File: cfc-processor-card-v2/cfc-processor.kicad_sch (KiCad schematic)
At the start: 11 parts, among them J1 TFM-120-01-L-D-RA, J2 2-1734592-0, J3 J-SAMTEC-TFM-110-X1-XXX-D-RA, J4 Conn_01x04

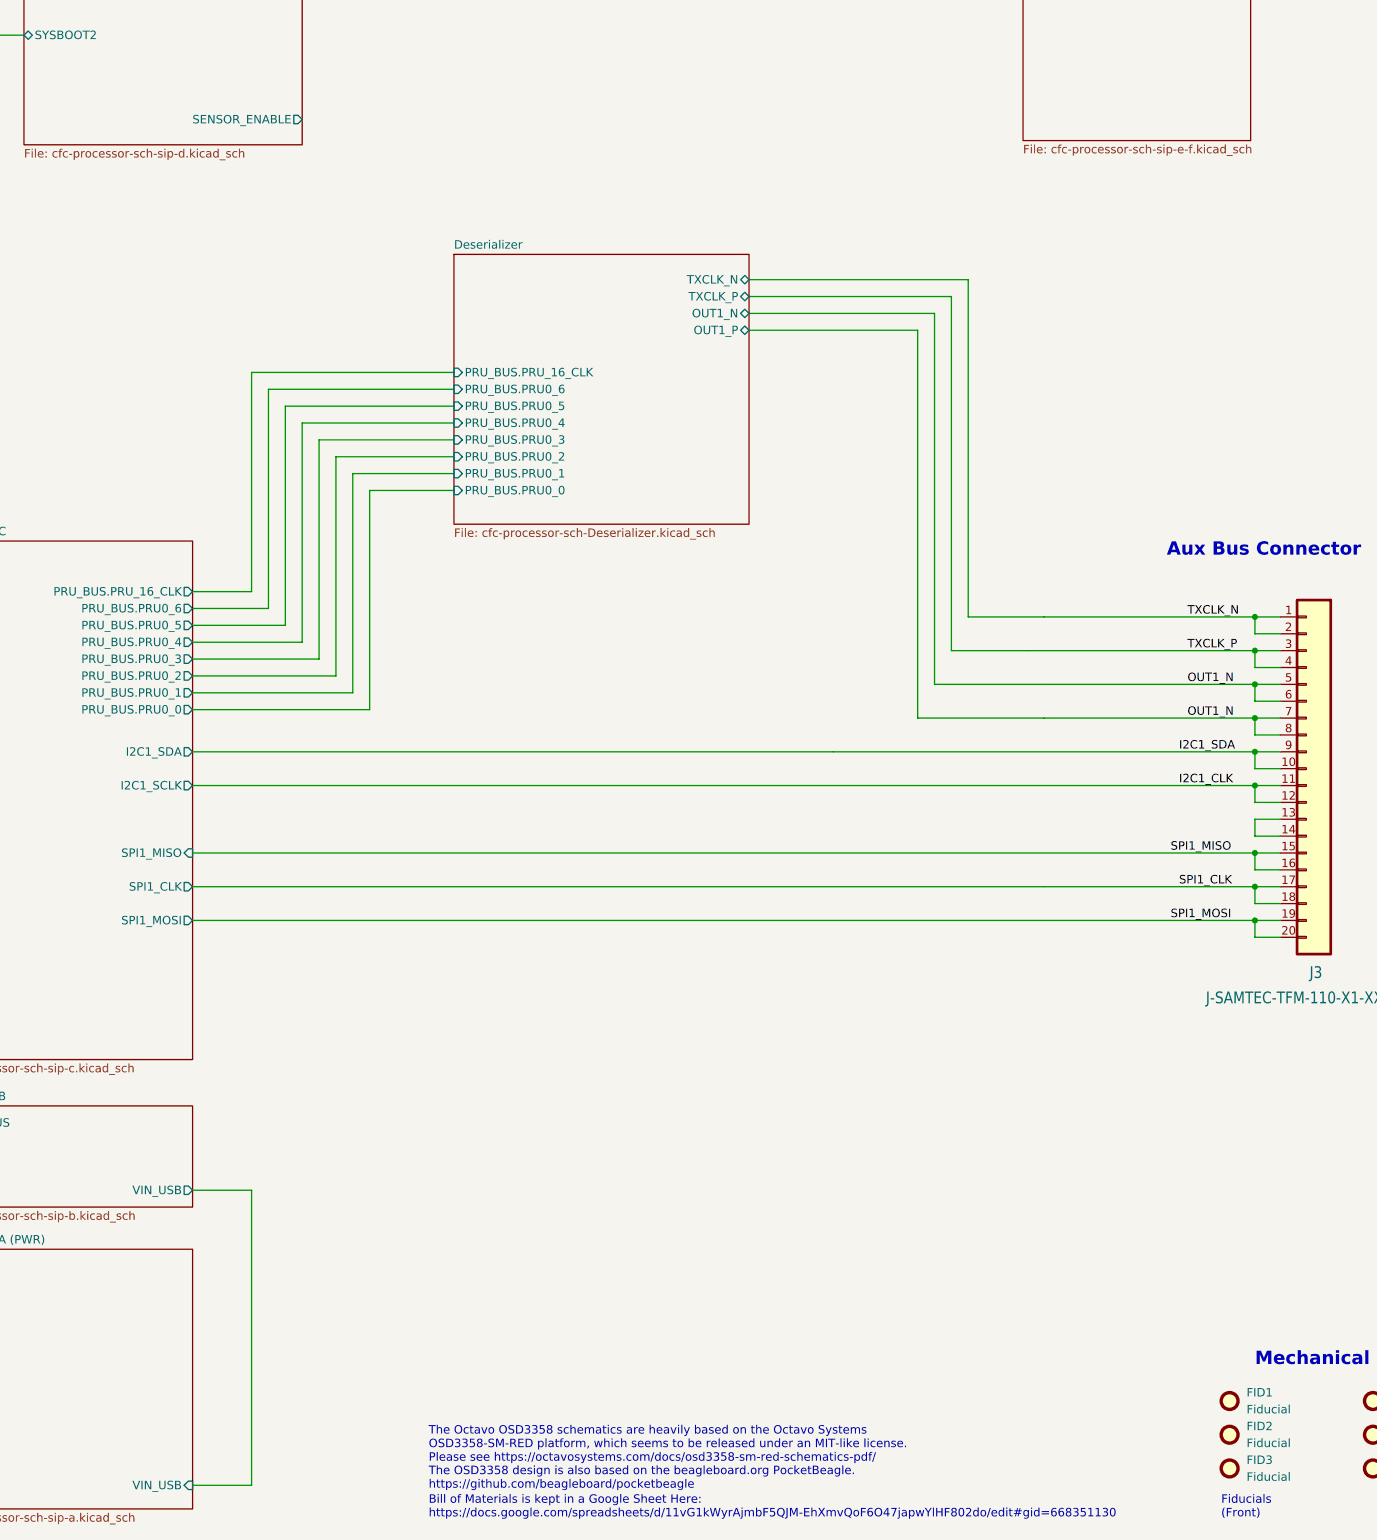
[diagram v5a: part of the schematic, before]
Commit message: Update
Added bidirectional TEC control with DRV8212 IC. Added Sensor enable pin back to processor; in case of i2c hang up octavo can still disable sensor.
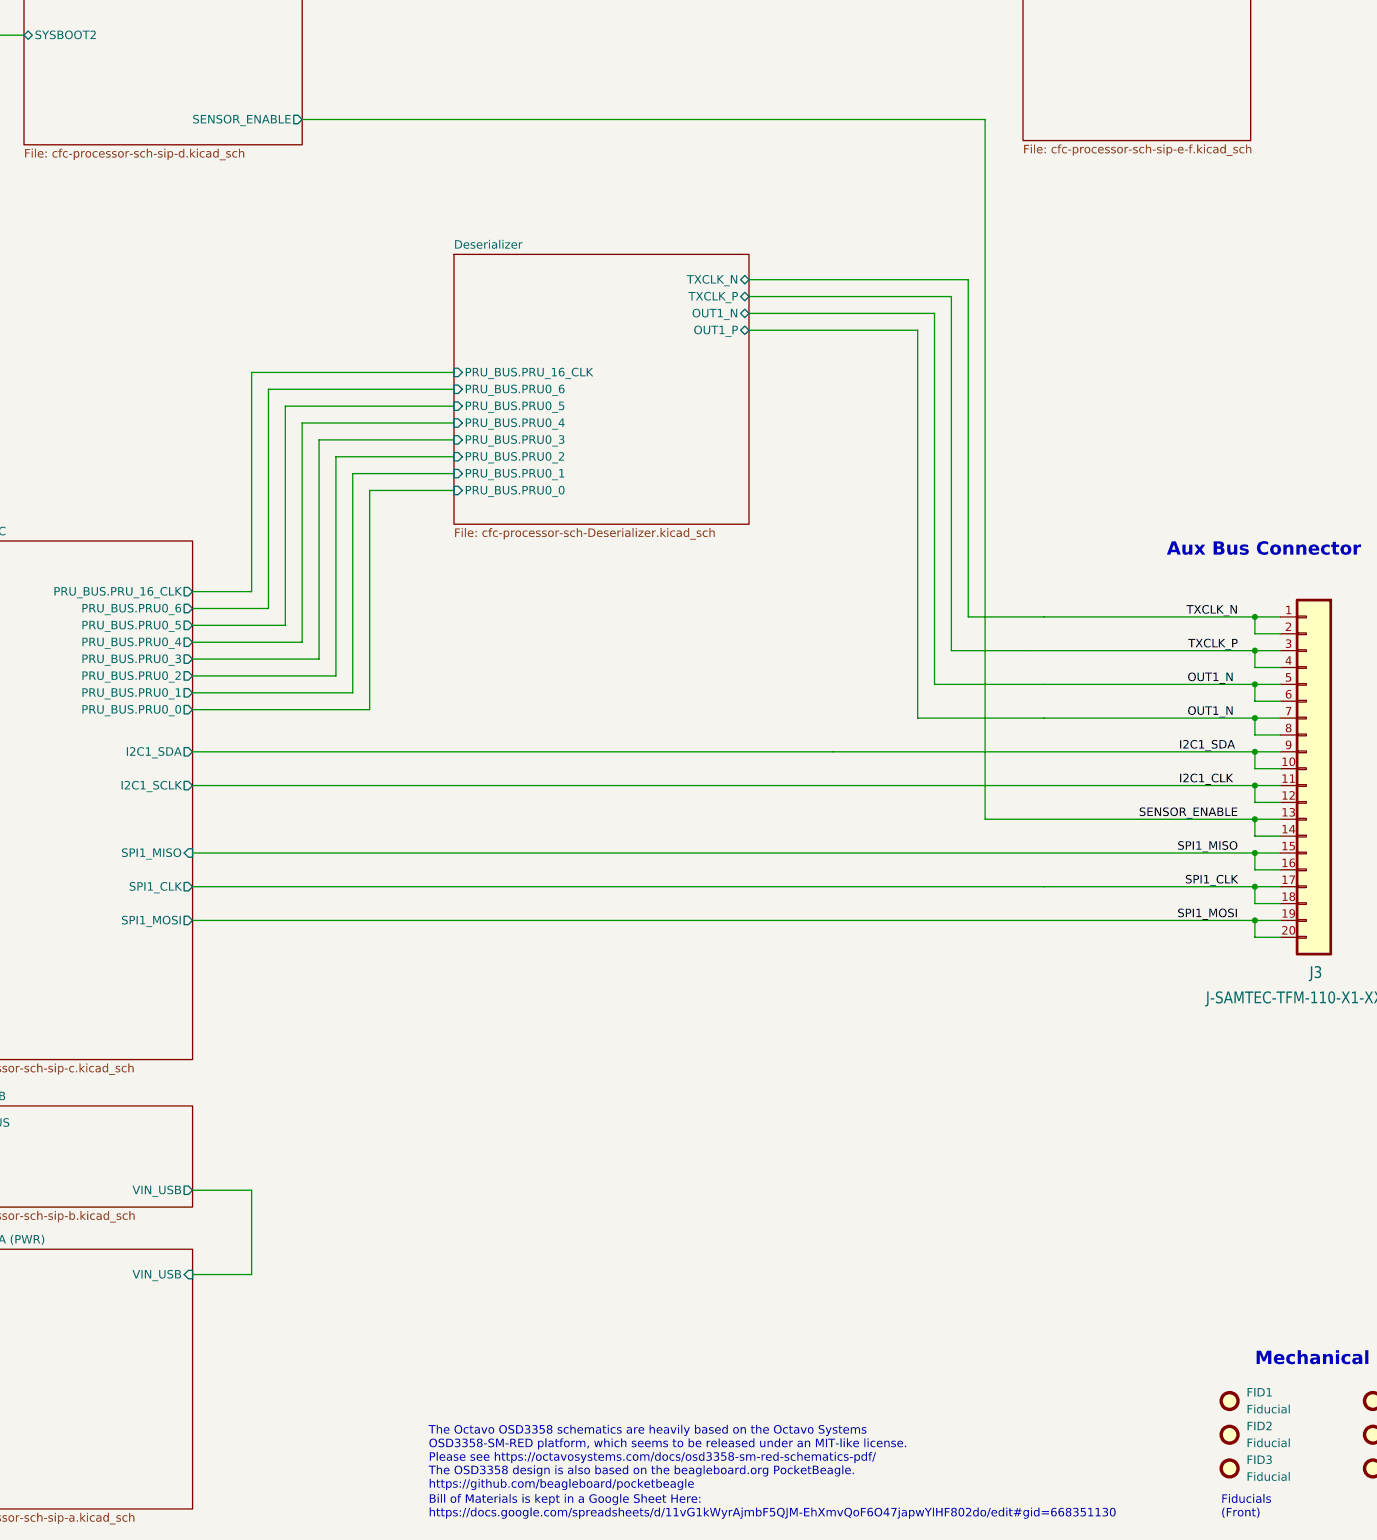
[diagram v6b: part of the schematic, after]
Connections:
- net SENSOR_ENABLE: now reaches J3.13, J3.14
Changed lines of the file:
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@@
 	)
 	(junction
+		(at 388.62 157.48)
+		(diameter 0)
+		(color 0 0 0 0)
+	)
+	(junction
 		(at 113.03 191.77)
 		(diameter 0)
@@
 	(wire
 		(pts
+			(xy 347.98 157.48) (xy 388.62 157.48)
+		)
+		(stroke
+			(width 0)
+			(type default)
+		)
+	)
+	(wire
+		(pts
 			(xy 388.62 139.7) (xy 392.43 139.7)
 		)
@@
 	(wire
 		(pts
-			(xy 228.6 257.81) (xy 237.49 257.81)
+			(xy 228.6 226.06) (xy 237.49 226.06)
 		)
 		(stroke
@@
 	(wire
 		(pts
+			(xy 245.11 52.07) (xy 347.98 52.07)
+		)
+		(stroke
+			(width 0)
+			(type default)
+		)
+	)
+	(wire
+		(pts
 			(xy 46.99 69.85) (xy 43.18 69.85)
 		)
@@
 	(wire
 		(pts
-			(xy 237.49 257.81) (xy 237.49 213.36)
+			(xy 237.49 226.06) (xy 237.49 213.36)
 		)
 		(stroke
@@
 	(wire
 		(pts
+			(xy 347.98 52.07) (xy 347.98 157.48)
+		)
+		(stroke
+			(width 0)
+			(type default)
+		)
+	)
+	(wire
+		(pts
 			(xy 95.25 176.53) (xy 95.25 224.79)
 		)
@@
 	)
 	(label "TXCLK_N"
-		(at 378.46 127 0)
+		(at 386.08 127 180)
 		(effects
 			(font
 				(size 1.27 1.27)
 			)
-			(justify left bottom)
+			(justify right bottom)
 		)
 	)
@@
 	)
 	(label "SPI1_CLK"
-		(at 377.19 167.64 0)
+		(at 386.08 167.64 180)
 		(effects
 			(font
 				(size 1.27 1.27)
 			)
-			(justify left bottom)
+			(justify right bottom)
 		)
 	)
 	(label "SPI1_MISO"
-		(at 375.92 162.56 0)
+		(at 386.08 162.56 180)
 		(effects
 			(font
 				(size 1.27 1.27)
 			)
-			(justify left bottom)
+			(justify right bottom)
 		)
 	)
@@
 		)
 	)
+	(label "SENSOR_ENABLE"
+		(at 386.08 157.48 180)
+		(effects
+			(font
+				(size 1.27 1.27)
+			)
+			(justify right bottom)
+		)
+	)
 	(label "C3-UART-TX"
 		(at 46.99 123.19 0)
@@
 	)
 	(label "SPI1_MOSI"
-		(at 375.92 172.72 0)
+		(at 386.08 172.72 180)
 		(effects
 			(font
 				(size 1.27 1.27)
 			)
-			(justify left bottom)
+			(justify right bottom)
 		)
 	)
 	(label "TXCLK_P"
-		(at 378.46 132.08 0)
+		(at 386.08 132.08 180)
 		(effects
 			(font
 				(size 1.27 1.27)
 			)
-			(justify left bottom)
+			(justify right bottom)
 		)
 	)
@@
 		)
 		(pin "VIN_USB" input
-			(at 228.6 257.81 0)
+			(at 228.6 226.06 0)
 			(effects
 				(font
